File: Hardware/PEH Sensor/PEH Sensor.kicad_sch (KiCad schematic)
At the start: 45 parts, among them J1 JST-XH-A B3B, Q1 AO3401A, SW1 JS202011JCQN, U1 SHTC3, U2 BQ25570, U3 VEML7700-TR, U4 INA226, U5 ESP32S3 Super Mini

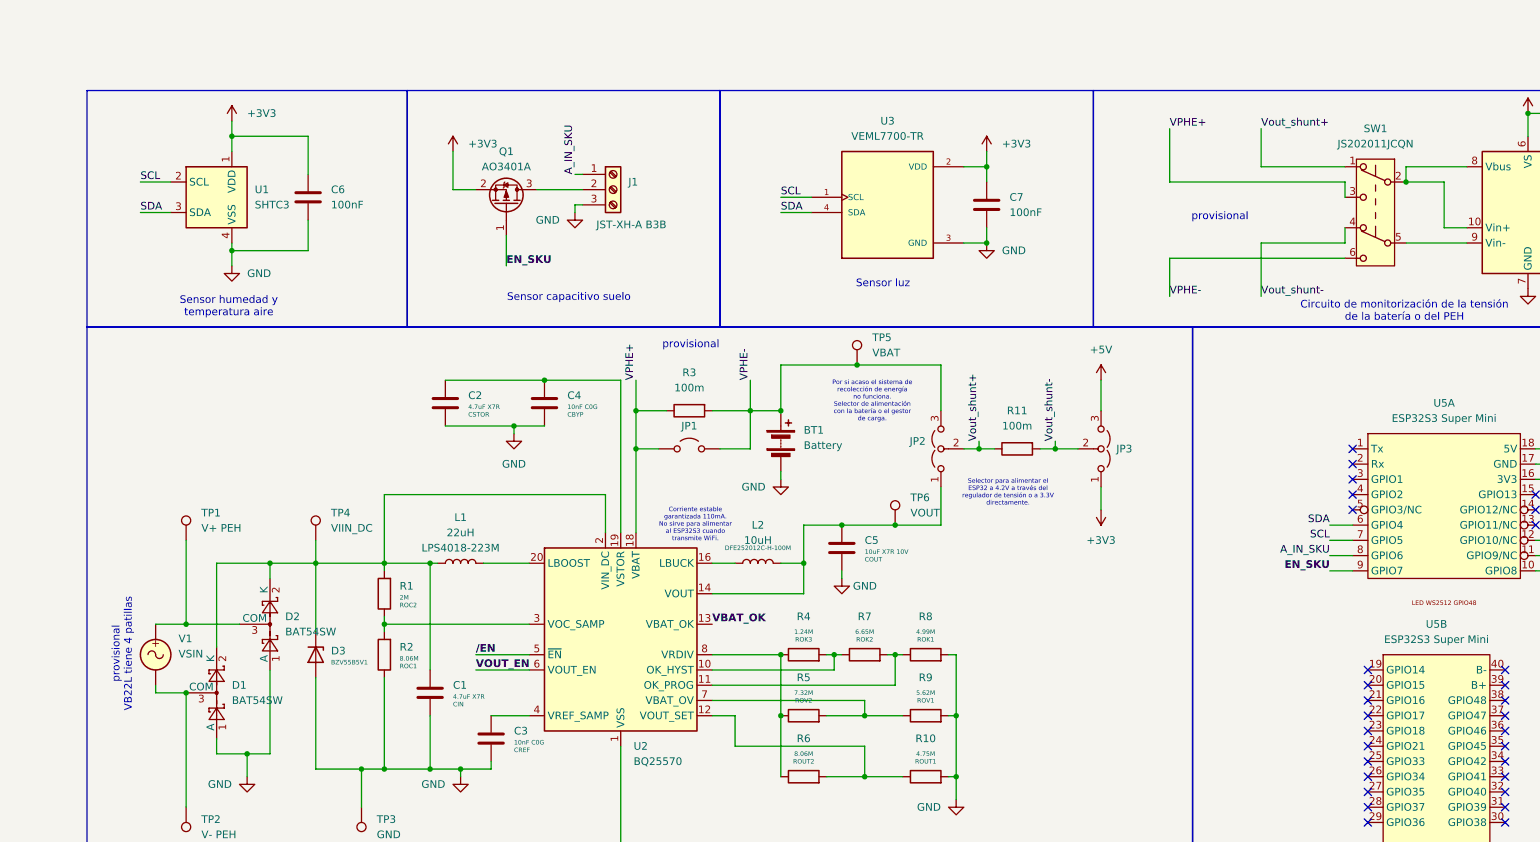
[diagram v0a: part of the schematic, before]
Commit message: Several PCB updates to hardware. Started BLE app on androidstudio.
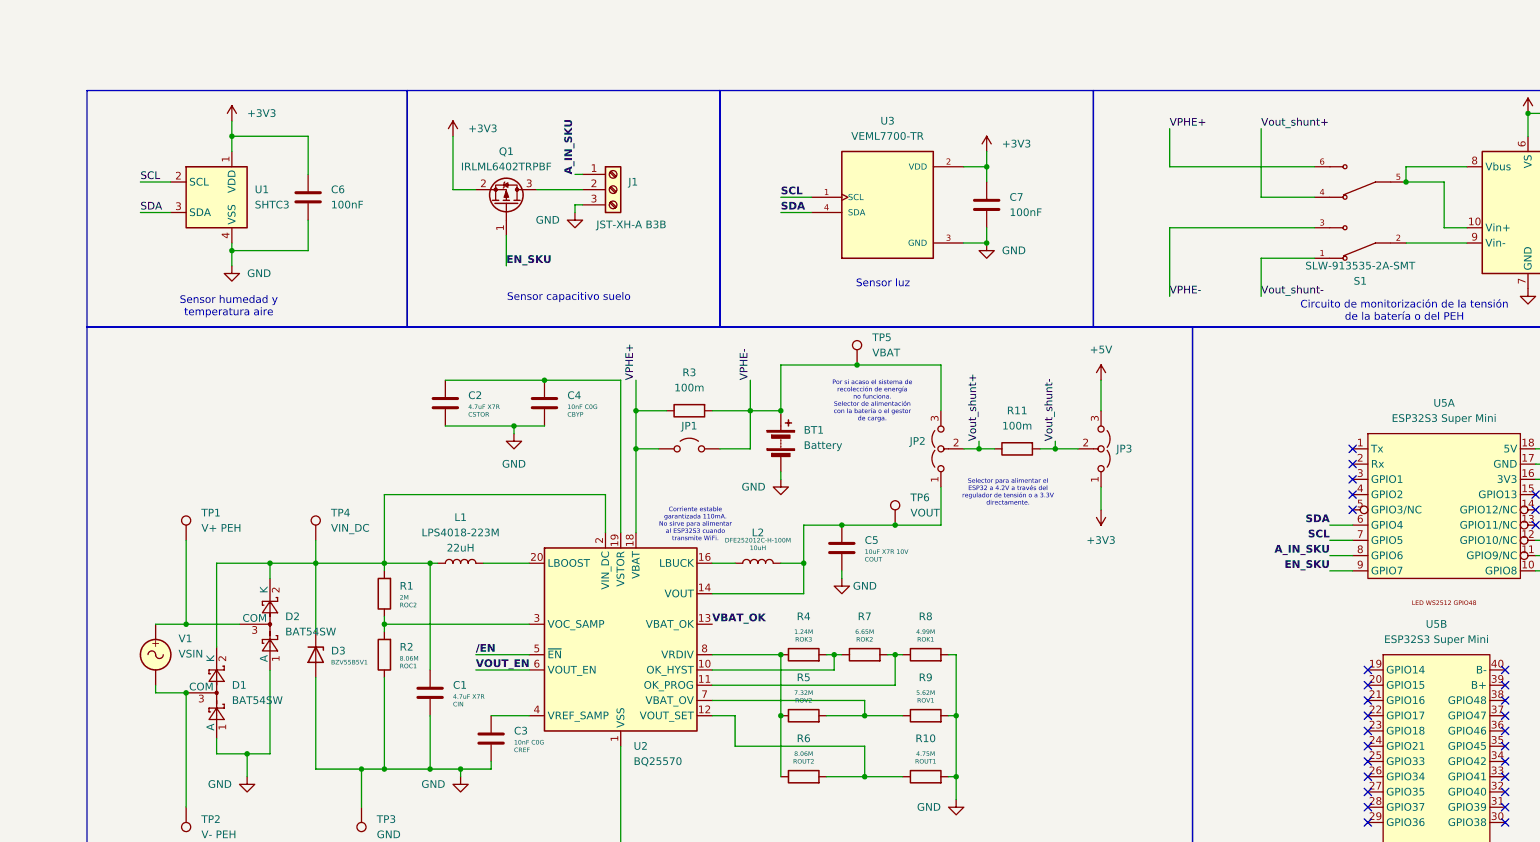
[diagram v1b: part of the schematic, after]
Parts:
- removed SW1: JS202011JCQN, Button_Switch_SMD:SW_DPDT_CK_JS202011JCQN, symbol Switch:SW_Push_DPDT
- added S1: SLW-913535-2A-SMT, SLW-913535-2A-SMT:SW_SLW-913535-2A-SMT, symbol SLW-913535-2A-SMT:SLW-913535-2A-SMT
- JP1, TP1, TP2, TP3, TP5, TP6: now left out of the parts list
- L1: value 22uH -> LPS4018-223M; Posible valor LPS4018-223M -> 22uH
- L2: value 10uH -> DFE252012C-H-100M; Posible valor DFE252012C-H-100M -> 10uH
- Q1: value AO3401A -> IRLML6402TRPBF
- TP4: Desc VIIN_DC -> VIN_DC; now left out of the parts list
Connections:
- net VPHE+: now also S1.6
- net VPHE-: now also S1.3
- net Vout_shunt+: now also S1.4
- net Vout_shunt-: now also S1.1
- net at U4.10 (Vin+), U4.8 (Vbus): now also S1.5
- net at U4.9 (Vin-): now also S1.2
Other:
- note removed: "provisional"
- note removed: "provisional VB22L tiene 4 patillas"

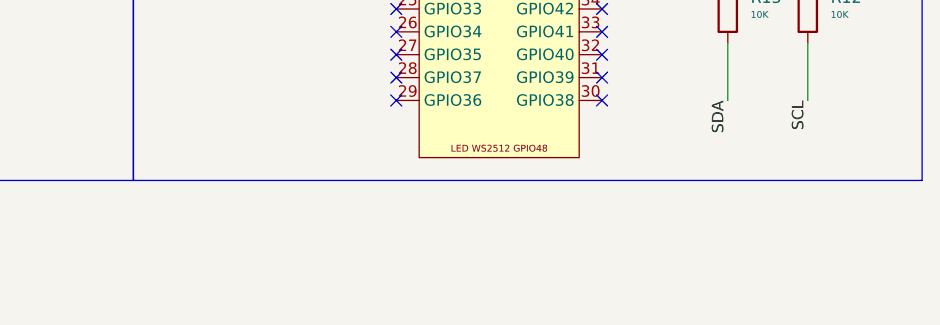
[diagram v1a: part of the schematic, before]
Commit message: Programa de prueba de sensores y actualización de PCB con cambio en la librería del VEML770
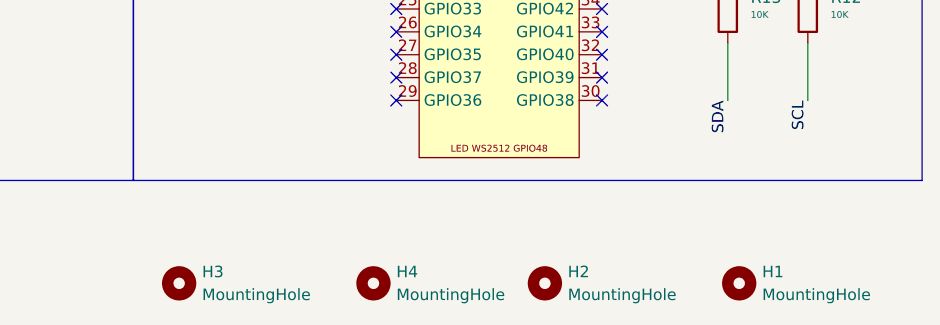
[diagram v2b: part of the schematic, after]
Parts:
- added H1, H2, H3, H4: MountingHole, MountingHole:MountingHole_3.2mm_M3_DIN965, symbol Mechanical:MountingHole
